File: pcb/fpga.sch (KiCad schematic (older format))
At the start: 45 parts, among them J1 CONN_INTEGRALSTICK_FPGA_DEVICE, Q1 SSM6N58NU, Q2 SSM6N58NU, Q3 SSM6N58NU, U12 DSC6001HI2A-025.0000‎, U2 XC7A50T-1FTG256C, U9 AT24MAC402-UDFN

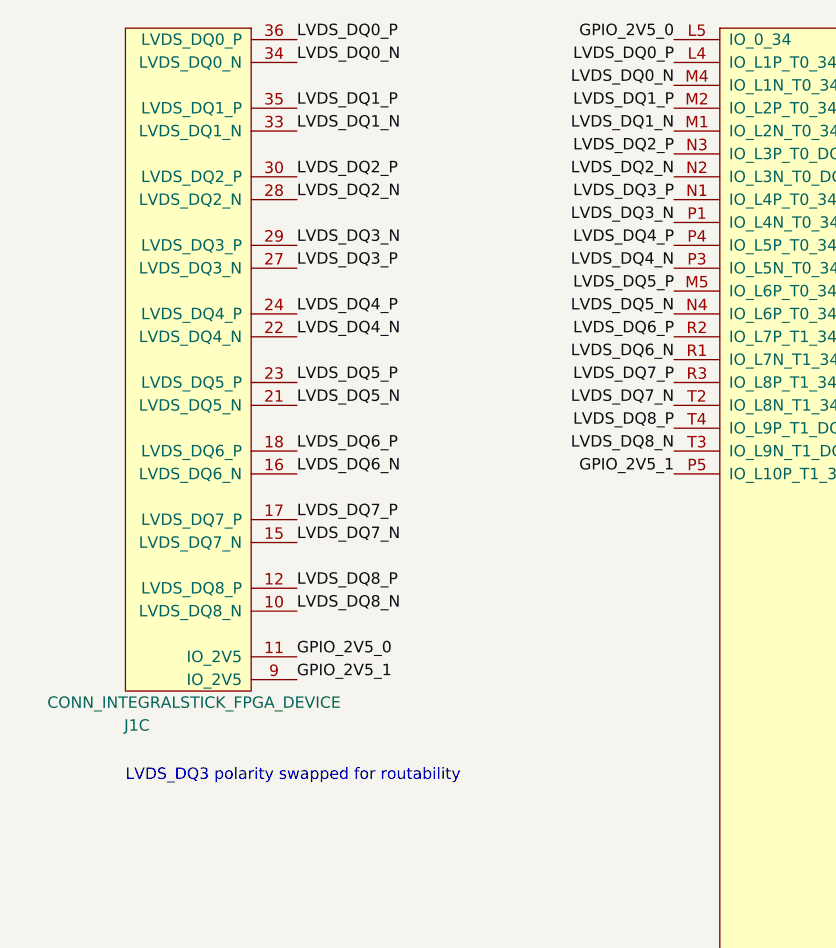
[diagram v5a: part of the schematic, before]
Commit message: Initial layout of LVDS bank
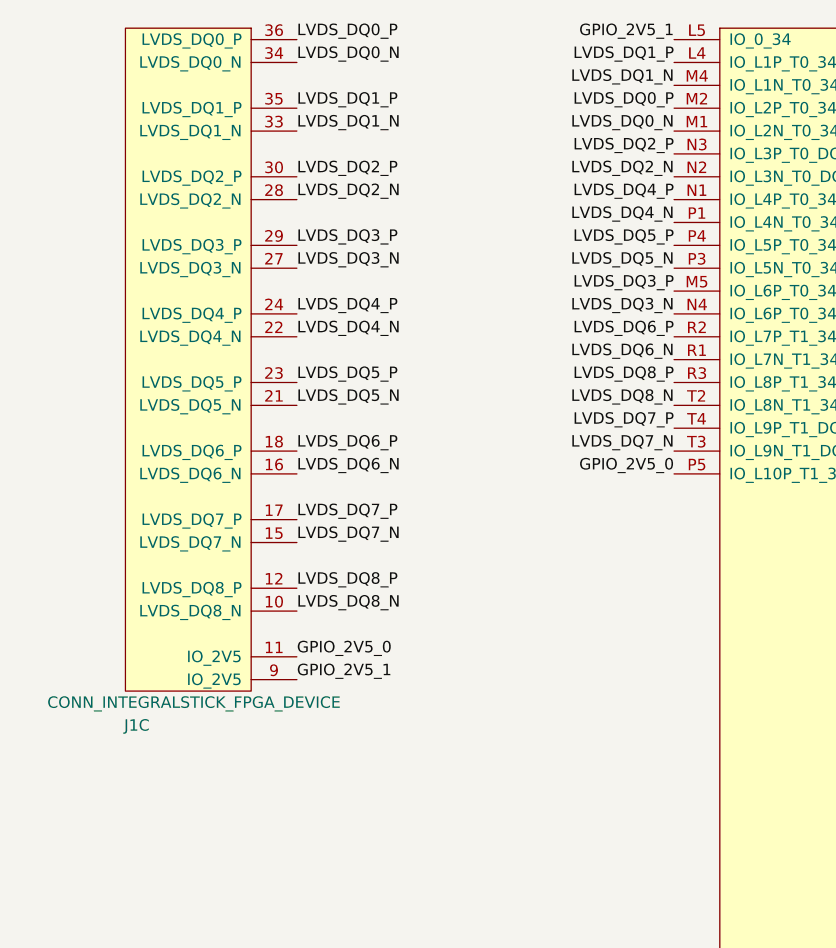
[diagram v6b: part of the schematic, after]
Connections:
- net GPIO_2V5_0: now also U2.P5 (IO_L10P_T1_34); no longer U2.L5 (IO_0_34)
- net GPIO_2V5_1: now also U2.L5 (IO_0_34); no longer U2.P5 (IO_L10P_T1_34)
- net LVDS_DQ0_N: now also U2.M1 (IO_L2N_T0_34); no longer U2.M4 (IO_L1N_T0_34)
- net LVDS_DQ0_P: now also U2.M2 (IO_L2P_T0_34); no longer U2.L4 (IO_L1P_T0_34)
- net LVDS_DQ1_N: now also U2.M4 (IO_L1N_T0_34); no longer U2.M1 (IO_L2N_T0_34)
- net LVDS_DQ1_P: now also U2.L4 (IO_L1P_T0_34); no longer U2.M2 (IO_L2P_T0_34)
- net LVDS_DQ3_N: now also J1.27 (LVDS_DQ3_N), U2.N4 (IO_L6P_T0_34); no longer J1.29 (LVDS_DQ3_P), U2.P1 (IO_L4N_T0_34)
- net LVDS_DQ3_P: now also J1.29 (LVDS_DQ3_P), U2.M5 (IO_L6P_T0_34); no longer J1.27 (LVDS_DQ3_N), U2.N1 (IO_L4P_T0_34)
- net LVDS_DQ4_N: now also U2.P1 (IO_L4N_T0_34); no longer U2.P3 (IO_L5N_T0_34)
- net LVDS_DQ4_P: now also U2.N1 (IO_L4P_T0_34); no longer U2.P4 (IO_L5P_T0_34)
- net LVDS_DQ5_N: now also U2.P3 (IO_L5N_T0_34); no longer U2.N4 (IO_L6P_T0_34)
- net LVDS_DQ5_P: now also U2.P4 (IO_L5P_T0_34); no longer U2.M5 (IO_L6P_T0_34)
- net LVDS_DQ7_N: now also U2.T3 (IO_L9N_T1_DQS_34); no longer U2.T2 (IO_L8N_T1_34)
- net LVDS_DQ7_P: now also U2.T4 (IO_L9P_T1_DQS_34); no longer U2.R3 (IO_L8P_T1_34)
- net LVDS_DQ8_N: now also U2.T2 (IO_L8N_T1_34); no longer U2.T3 (IO_L9N_T1_DQS_34)
- net LVDS_DQ8_P: now also U2.R3 (IO_L8P_T1_34); no longer U2.T4 (IO_L9P_T1_DQS_34)
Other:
- note removed: "LVDS_DQ3 polarity swapped for routability"
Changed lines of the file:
@@
 	-1   0    0    -1
 $EndComp
+Text Label 3300 2650 2    50   ~ 0
+GPIO_2V5_0
 Text Label 3300 750  2    50   ~ 0
-GPIO_2V5_0
-Text Label 3300 2650 2    50   ~ 0
 GPIO_2V5_1
 Text Label 1650 3550 0    50   ~ 0
@@
 Text Label 1650 3450 0    50   ~ 0
 GPIO_2V5_0
+Text Label 3300 1050 2    50   ~ 0
+LVDS_DQ0_P
+Text Label 3300 1150 2    50   ~ 0
+LVDS_DQ0_N
 Text Label 3300 850  2    50   ~ 0
-LVDS_DQ0_P
+LVDS_DQ1_P
 Text Label 3300 950  2    50   ~ 0
-LVDS_DQ0_N
-Text Label 3300 1050 2    50   ~ 0
-LVDS_DQ1_P
-Text Label 3300 1150 2    50   ~ 0
 LVDS_DQ1_N
 Text Label 3300 1250 2    50   ~ 0
@@
 Text Label 3300 1350 2    50   ~ 0
 LVDS_DQ2_N
+Text Label 3300 1850 2    50   ~ 0
+LVDS_DQ3_P
+Text Label 3300 1950 2    50   ~ 0
+LVDS_DQ3_N
 Text Label 3300 1450 2    50   ~ 0
-LVDS_DQ3_P
+LVDS_DQ4_P
 Text Label 3300 1550 2    50   ~ 0
-LVDS_DQ3_N
+LVDS_DQ4_N
 Text Label 3300 1650 2    50   ~ 0
-LVDS_DQ4_P
+LVDS_DQ5_P
 Text Label 3300 1750 2    50   ~ 0
-LVDS_DQ4_N
-Text Label 3300 1850 2    50   ~ 0
-LVDS_DQ5_P
-Text Label 3300 1950 2    50   ~ 0
 LVDS_DQ5_N
 Text Label 3300 2050 2    50   ~ 0
@@
 Text Label 3300 2150 2    50   ~ 0
 LVDS_DQ6_N
+Text Label 3300 2450 2    50   ~ 0
+LVDS_DQ7_P
+Text Label 3300 2550 2    50   ~ 0
+LVDS_DQ7_N
 Text Label 3300 2250 2    50   ~ 0
-LVDS_DQ7_P
+LVDS_DQ8_P
 Text Label 3300 2350 2    50   ~ 0
-LVDS_DQ7_N
-Text Label 3300 2450 2    50   ~ 0
-LVDS_DQ8_P
-Text Label 3300 2550 2    50   ~ 0
 LVDS_DQ8_N
 Text Label 1650 750  0    50   ~ 0
@@
 Text Label 1650 1450 0    50   ~ 0
 LVDS_DQ2_N
+Text Label 1650 1650 0    50   ~ 0
+LVDS_DQ3_P
 Text Label 1650 1750 0    50   ~ 0
-LVDS_DQ3_P
-Text Label 1650 1650 0    50   ~ 0
 LVDS_DQ3_N
 Text Label 1650 1950 0    50   ~ 0
@@
 $EndComp
 NoConn ~ 8400 2950
-Text Notes 900  4000 0    50   ~ 0
-LVDS_DQ3 polarity swapped for routability
 NoConn ~ 8400 3850
 NoConn ~ 8400 3550

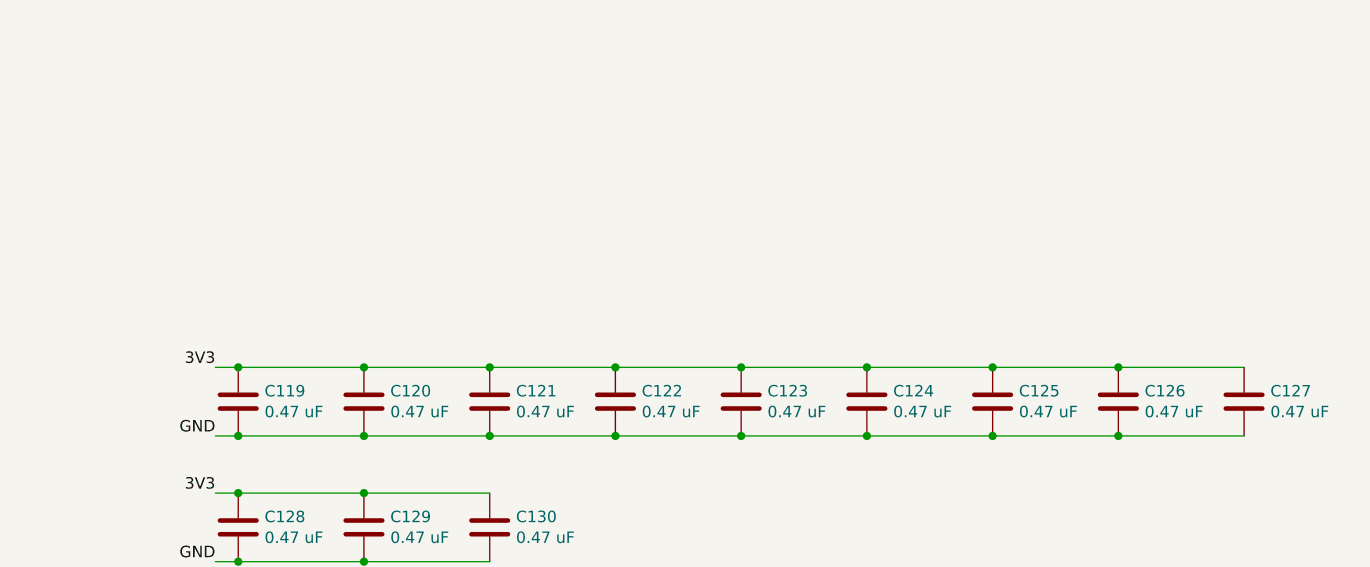
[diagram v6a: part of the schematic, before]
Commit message: Added missing 1V8 clock. Tweaked planes. Added some layer change caps.
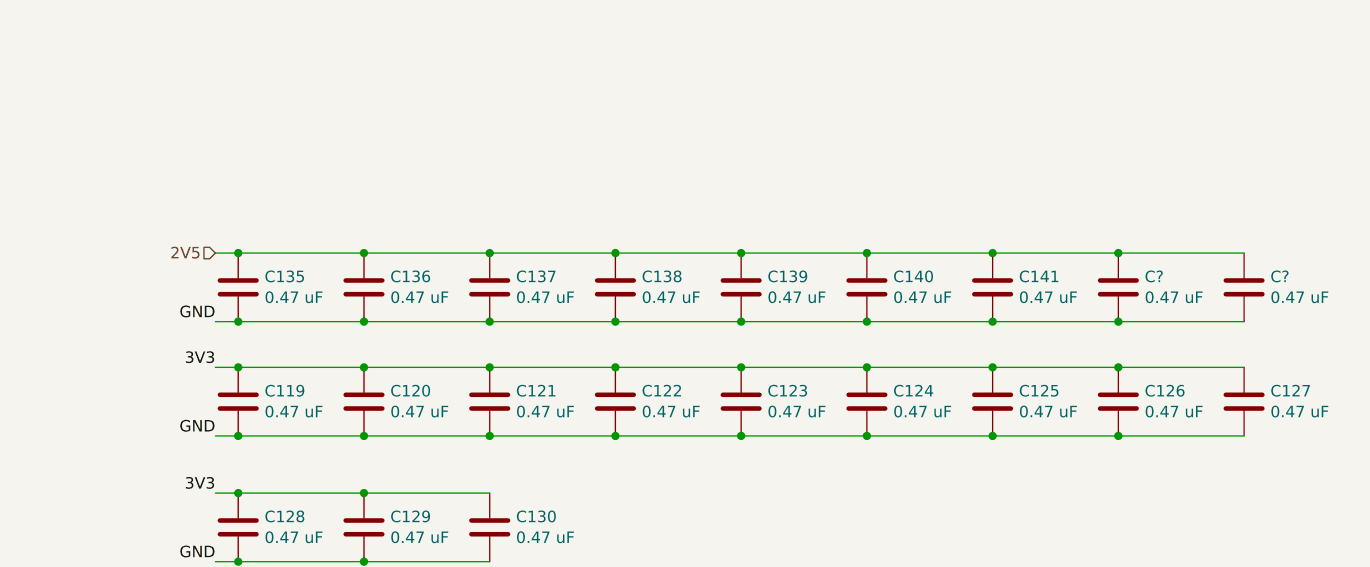
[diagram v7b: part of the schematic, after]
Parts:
- added C135, C136, C137, C138, C139, C140, C141, C? (x2): 0.47 uF, azonenberg_pcb:EIA_0402_CAP_NOSILK, symbol device:C
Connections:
- net GND: now also C135.2, C136.2, C137.2, C138.2, C139.2, C140.2, C141.2, C?.2, C?.2
- new net 2V5: C135.1, C136.1, C137.1, C138.1, C139.1, C140.1, C141.1, C?.1, C?.1
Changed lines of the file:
@@
 Text HLabel 11100 9300 0    50   Input ~ 0
 1V8
+Text HLabel 11100 7750 0    50   Input ~ 0
+2V5
+$Comp
+L device:C C?
+U 1 1 5C3BE3B1
+P 11200 7900
+AR Path="/5B6B7044/5C3BE3B1" Ref="C?"  Part="1"
+AR Path="/5B6B702C/5C3BE3B1" Ref="C135"  Part="1"
+F 0 "C135" H 11315 7946 50  0000 L CNN
+F 1 "0.47 uF" H 11315 7855 50  0000 L CNN
+F 2 "azonenberg_pcb:EIA_0402_CAP_NOSILK" H 11238 7750 50  0001 C CNN
+F 3 "" H 11200 7900 50  0001 C CNN
+	1    11200 7900
+	1    0    0    -1
+$EndComp
+Text Label 11100 8050 2    50   ~ 0
+GND
+Wire Wire Line
+	11100 7750 11200 7750
+Wire Wire Line
+	11100 8050 11200 8050
+$Comp
+L device:C C?
+U 1 1 5C3C73D2
+P 11750 7900
+AR Path="/5B6B7044/5C3C73D2" Ref="C?"  Part="1"
+AR Path="/5B6B702C/5C3C73D2" Ref="C136"  Part="1"
+F 0 "C136" H 11865 7946 50  0000 L CNN
+F 1 "0.47 uF" H 11865 7855 50  0000 L CNN
+F 2 "azonenberg_pcb:EIA_0402_CAP_NOSILK" H 11788 7750 50  0001 C CNN
+F 3 "" H 11750 7900 50  0001 C CNN
+	1    11750 7900
+	1    0    0    -1
+$EndComp
+$Comp
+L device:C C?
+U 1 1 5C3C776E
+P 12300 7900
+AR Path="/5B6B7044/5C3C776E" Ref="C?"  Part="1"
+AR Path="/5B6B702C/5C3C776E" Ref="C137"  Part="1"
+F 0 "C137" H 12415 7946 50  0000 L CNN
+F 1 "0.47 uF" H 12415 7855 50  0000 L CNN
+F 2 "azonenberg_pcb:EIA_0402_CAP_NOSILK" H 12338 7750 50  0001 C CNN
+F 3 "" H 12300 7900 50  0001 C CNN
+	1    12300 7900
+	1    0    0    -1
+$EndComp
+Wire Wire Line
+	12300 7750 11750 7750
+Connection ~ 11200 7750
+Connection ~ 11750 7750
+Wire Wire Line
+	11750 7750 11200 7750
+Wire Wire Line
+	11200 8050 11750 8050
+Connection ~ 11200 8050
+Connection ~ 11750 8050
+Wire Wire Line
+	11750 8050 12300 8050
+$Comp
+L device:C C?
+U 1 1 5C3CEED6
+P 12850 7900
+AR Path="/5B6B7044/5C3CEED6" Ref="C?"  Part="1"
+AR Path="/5B6B702C/5C3CEED6" Ref="C138"  Part="1"
+F 0 "C138" H 12965 7946 50  0000 L CNN
+F 1 "0.47 uF" H 12965 7855 50  0000 L CNN
+F 2 "azonenberg_pcb:EIA_0402_CAP_NOSILK" H 12888 7750 50  0001 C CNN
+F 3 "" H 12850 7900 50  0001 C CNN
+	1    12850 7900
+	1    0    0    -1
+$EndComp
+$Comp
+L device:C C?
+U 1 1 5C3CF2B1
+P 13400 7900
+AR Path="/5B6B7044/5C3CF2B1" Ref="C?"  Part="1"
+AR Path="/5B6B702C/5C3CF2B1" Ref="C139"  Part="1"
+F 0 "C139" H 13515 7946 50  0000 L CNN
+F 1 "0.47 uF" H 13515 7855 50  0000 L CNN
+F 2 "azonenberg_pcb:EIA_0402_CAP_NOSILK" H 13438 7750 50  0001 C CNN
+F 3 "" H 13400 7900 50  0001 C CNN
+	1    13400 7900
+	1    0    0    -1
+$EndComp
+Wire Wire Line
+	13400 7750 12850 7750
+Connection ~ 12300 7750
+Connection ~ 12850 7750
+Wire Wire Line
+	12850 7750 12300 7750
+Wire Wire Line
+	13400 8050 12850 8050
+Connection ~ 12300 8050
+Connection ~ 12850 8050
+Wire Wire Line
+	12850 8050 12300 8050
+$Comp
+L device:C C?
+U 1 1 5C3D7589
+P 13950 7900
+AR Path="/5B6B7044/5C3D7589" Ref="C?"  Part="1"
+AR Path="/5B6B702C/5C3D7589" Ref="C140"  Part="1"
+F 0 "C140" H 14065 7946 50  0000 L CNN
+F 1 "0.47 uF" H 14065 7855 50  0000 L CNN
+F 2 "azonenberg_pcb:EIA_0402_CAP_NOSILK" H 13988 7750 50  0001 C CNN
+F 3 "" H 13950 7900 50  0001 C CNN
+	1    13950 7900
+	1    0    0    -1
+$EndComp
+$Comp
+L device:C C?
+U 1 1 5C3D7AE6
+P 14500 7900
+AR Path="/5B6B7044/5C3D7AE6" Ref="C?"  Part="1"
+AR Path="/5B6B702C/5C3D7AE6" Ref="C141"  Part="1"
+F 0 "C141" H 14615 7946 50  0000 L CNN
+F 1 "0.47 uF" H 14615 7855 50  0000 L CNN
+F 2 "azonenberg_pcb:EIA_0402_CAP_NOSILK" H 14538 7750 50  0001 C CNN
+F 3 "" H 14500 7900 50  0001 C CNN
+	1    14500 7900
+	1    0    0    -1
+$EndComp
+Wire Wire Line
+	14500 7750 13950 7750
+Connection ~ 13400 7750
+Connection ~ 13950 7750
+Wire Wire Line
+	13950 7750 13400 7750
+Wire Wire Line
+	14500 8050 13950 8050
+Connection ~ 13400 8050
+Connection ~ 13950 8050
+Wire Wire Line
+	13950 8050 13400 8050
+$Comp
+L device:C C?
+U 1 1 5C3E05B4
+P 15050 7900
+AR Path="/5B6B7044/5C3E05B4" Ref="C?"  Part="1"
+AR Path="/5B6B702C/5C3E05B4" Ref="C?"  Part="1"
+F 0 "C?" H 15165 7946 50  0000 L CNN
+F 1 "0.47 uF" H 15165 7855 50  0000 L CNN
+F 2 "azonenberg_pcb:EIA_0402_CAP_NOSILK" H 15088 7750 50  0001 C CNN
+F 3 "" H 15050 7900 50  0001 C CNN
+	1    15050 7900
+	1    0    0    -1
+$EndComp
+$Comp
+L device:C C?
+U 1 1 5C3E0A0B
+P 15600 7900
+AR Path="/5B6B7044/5C3E0A0B" Ref="C?"  Part="1"
+AR Path="/5B6B702C/5C3E0A0B" Ref="C?"  Part="1"
+F 0 "C?" H 15715 7946 50  0000 L CNN
+F 1 "0.47 uF" H 15715 7855 50  0000 L CNN
+F 2 "azonenberg_pcb:EIA_0402_CAP_NOSILK" H 15638 7750 50  0001 C CNN
+F 3 "" H 15600 7900 50  0001 C CNN
+	1    15600 7900
+	1    0    0    -1
+$EndComp
+Wire Wire Line
+	15600 7750 15050 7750
+Connection ~ 14500 7750
+Connection ~ 15050 7750
+Wire Wire Line
+	15050 7750 14500 7750
+Wire Wire Line
+	14500 8050 15050 8050
+Connection ~ 14500 8050
+Connection ~ 15050 8050
+Wire Wire Line
+	15050 8050 15600 8050
 $EndSCHEMATC
